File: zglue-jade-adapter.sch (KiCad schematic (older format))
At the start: 63 parts, among them J1 543630489, J2 543630489

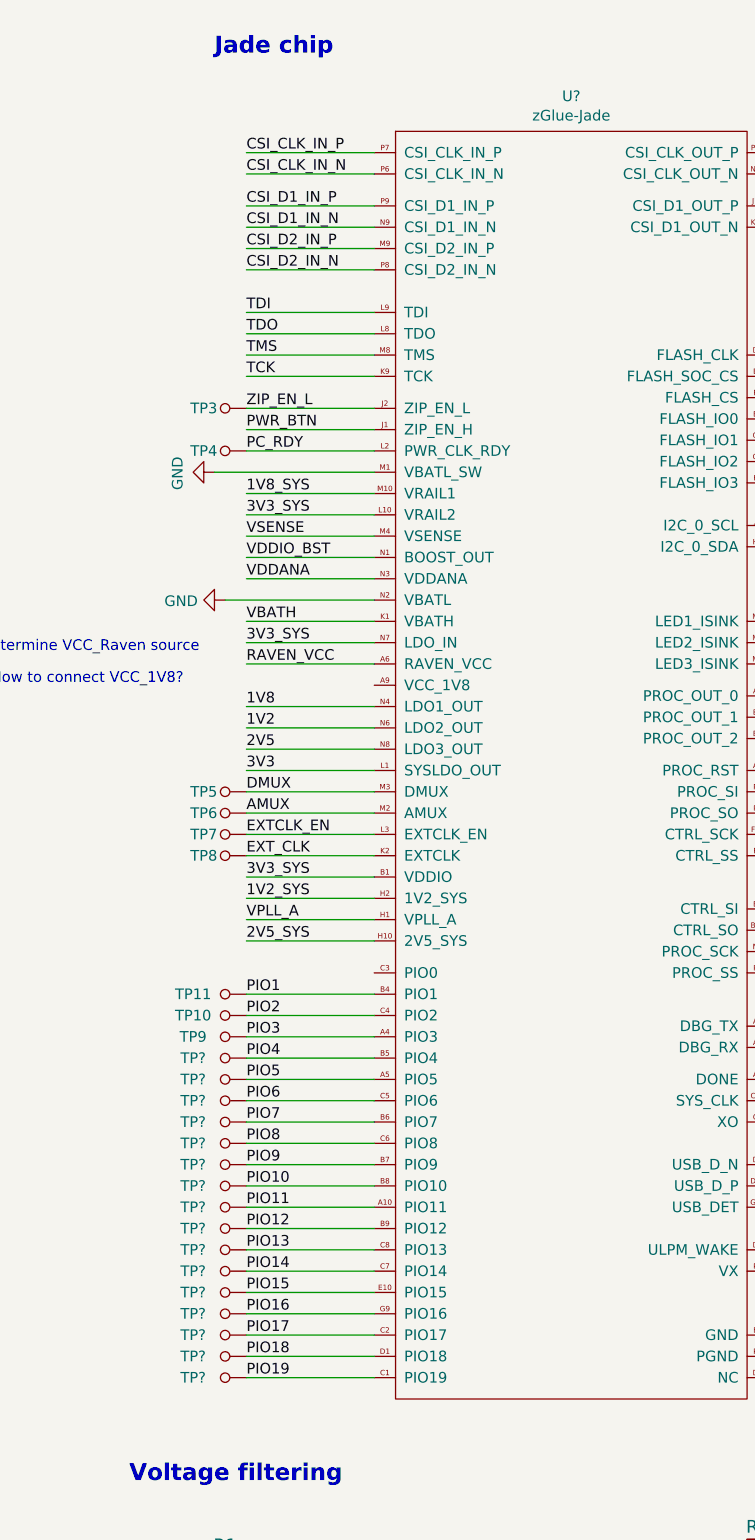
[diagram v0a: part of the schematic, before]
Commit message: Add component placement
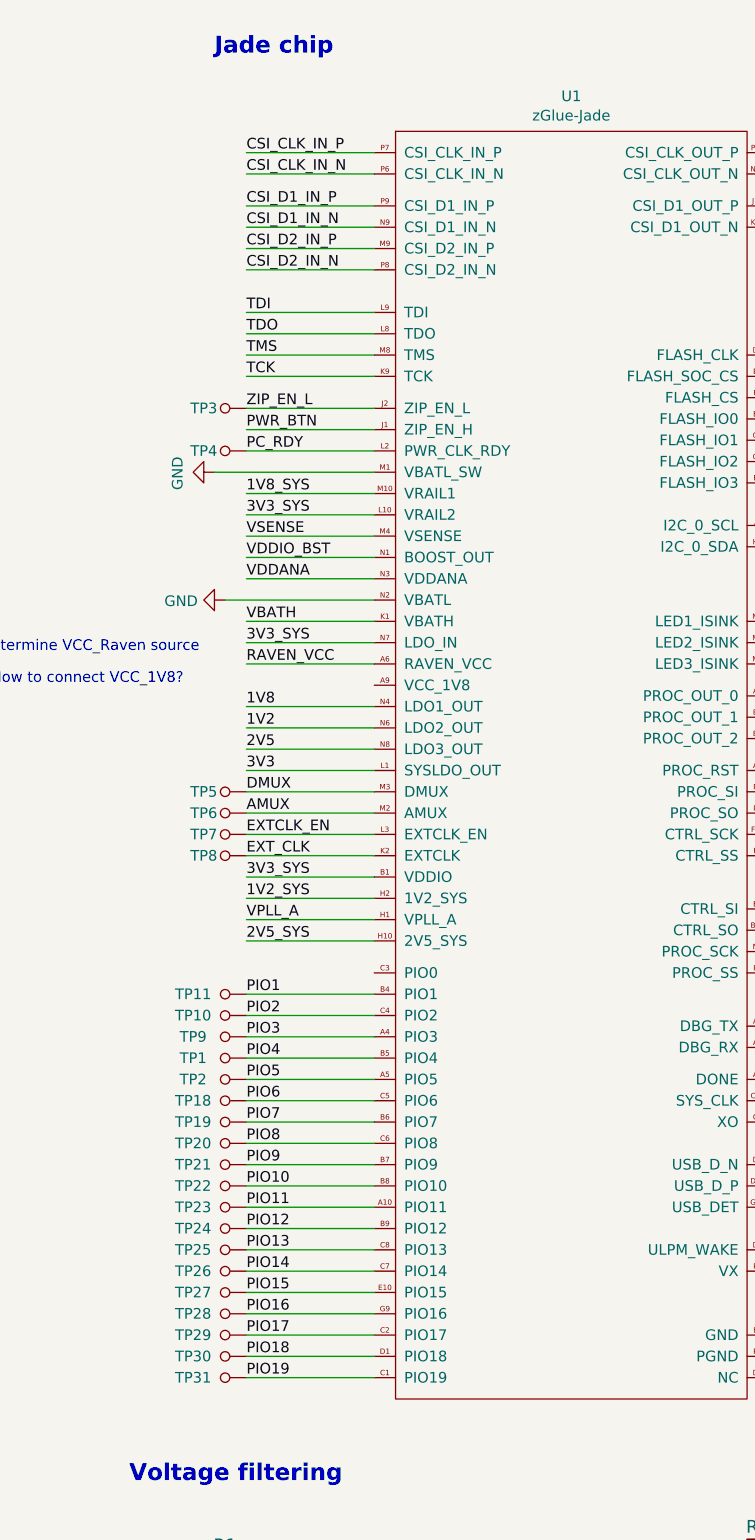
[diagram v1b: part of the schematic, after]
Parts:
- U1: renamed from U?; footprint (none) -> lib:Z-Glue_LGA-96
- gave numbers to parts that had none: 16
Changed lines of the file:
@@
 $EndComp
 $Comp
-L power:GND #PWR?
+L power:GND #PWR0101
 U 1 1 5DBC7F26
 P 1600 2800
-F 0 "#PWR?" H 1600 2550 50  0001 C CNN
+F 0 "#PWR0101" H 1600 2550 50  0001 C CNN
 F 1 "GND" H 1605 2627 50  0000 C CNN
 F 2 "" H 1600 2800 50  0001 C CNN
@@
 RAVEN_VCC
 $Comp
-L power:GND #PWR?
+L power:GND #PWR0102
 U 1 1 5E01A99B
 P 4450 7100
-F 0 "#PWR?" H 4450 6850 50  0001 C CNN
+F 0 "#PWR0102" H 4450 6850 50  0001 C CNN
 F 1 "GND" H 4455 6927 50  0000 C CNN
 F 2 "" H 4450 7100 50  0001 C CNN
@@
 	2350 5650 1750 5650
 $Comp
-L antmicroTestPoints:TP_SMD1MM TP?
+L antmicroTestPoints:TP_SMD1MM TP18
 U 1 1 5E08B0EF
 P 1650 5750
-F 0 "TP?" V 1650 5600 50  0000 C CNN
+F 0 "TP18" V 1650 5600 50  0000 C CNN
 F 1 "TP_SMD1MM" H 1650 5650 50  0001 C CNN
 F 2 "antmicro-footprints:Testpoint_smd_1mm" H 1850 5950 60  0001 L CNN
@@
 $EndComp
 $Comp
-L antmicroTestPoints:TP_SMD1MM TP?
+L antmicroTestPoints:TP_SMD1MM TP2
 U 1 1 5E08B0F6
 P 1650 5650
-F 0 "TP?" V 1650 5500 50  0000 C CNN
+F 0 "TP2" V 1650 5500 50  0000 C CNN
 F 1 "TP_SMD1MM" H 1650 5550 50  0001 C CNN
 F 2 "antmicro-footprints:Testpoint_smd_1mm" H 1850 5850 60  0001 L CNN
@@
 $EndComp
 $Comp
-L antmicroTestPoints:TP_SMD1MM TP?
+L antmicroTestPoints:TP_SMD1MM TP1
 U 1 1 5E08B0FD
 P 1650 5550
-F 0 "TP?" V 1650 5400 50  0000 C CNN
+F 0 "TP1" V 1650 5400 50  0000 C CNN
 F 1 "TP_SMD1MM" H 1650 5450 50  0001 C CNN
 F 2 "antmicro-footprints:Testpoint_smd_1mm" H 1850 5750 60  0001 L CNN
@@
 	2350 5950 1750 5950
 $Comp
-L antmicroTestPoints:TP_SMD1MM TP?
+L antmicroTestPoints:TP_SMD1MM TP21
 U 1 1 5E09E6BC
 P 1650 6050
-F 0 "TP?" V 1650 5900 50  0000 C CNN
+F 0 "TP21" V 1650 5900 50  0000 C CNN
 F 1 "TP_SMD1MM" H 1650 5950 50  0001 C CNN
 F 2 "antmicro-footprints:Testpoint_smd_1mm" H 1850 6250 60  0001 L CNN
@@
 $EndComp
 $Comp
-L antmicroTestPoints:TP_SMD1MM TP?
+L antmicroTestPoints:TP_SMD1MM TP20
 U 1 1 5E09E6C3
 P 1650 5950
-F 0 "TP?" V 1650 5800 50  0000 C CNN
+F 0 "TP20" V 1650 5800 50  0000 C CNN
 F 1 "TP_SMD1MM" H 1650 5850 50  0001 C CNN
 F 2 "antmicro-footprints:Testpoint_smd_1mm" H 1850 6150 60  0001 L CNN
@@
 $EndComp
 $Comp
-L antmicroTestPoints:TP_SMD1MM TP?
+L antmicroTestPoints:TP_SMD1MM TP19
 U 1 1 5E09E6CA
 P 1650 5850
-F 0 "TP?" V 1650 5700 50  0000 C CNN
+F 0 "TP19" V 1650 5700 50  0000 C CNN
 F 1 "TP_SMD1MM" H 1650 5750 50  0001 C CNN
 F 2 "antmicro-footprints:Testpoint_smd_1mm" H 1850 6050 60  0001 L CNN
@@
 	2350 6250 1750 6250
 $Comp
-L antmicroTestPoints:TP_SMD1MM TP?
+L antmicroTestPoints:TP_SMD1MM TP24
 U 1 1 5E0B2973
 P 1650 6350
-F 0 "TP?" V 1650 6200 50  0000 C CNN
+F 0 "TP24" V 1650 6200 50  0000 C CNN
 F 1 "TP_SMD1MM" H 1650 6250 50  0001 C CNN
 F 2 "antmicro-footprints:Testpoint_smd_1mm" H 1850 6550 60  0001 L CNN
@@
 $EndComp
 $Comp
-L antmicroTestPoints:TP_SMD1MM TP?
+L antmicroTestPoints:TP_SMD1MM TP23
 U 1 1 5E0B297A
 P 1650 6250
-F 0 "TP?" V 1650 6100 50  0000 C CNN
+F 0 "TP23" V 1650 6100 50  0000 C CNN
 F 1 "TP_SMD1MM" H 1650 6150 50  0001 C CNN
 F 2 "antmicro-footprints:Testpoint_smd_1mm" H 1850 6450 60  0001 L CNN
@@
 $EndComp
 $Comp
-L antmicroTestPoints:TP_SMD1MM TP?
+L antmicroTestPoints:TP_SMD1MM TP22
 U 1 1 5E0B2981
 P 1650 6150
-F 0 "TP?" V 1650 6000 50  0000 C CNN
+F 0 "TP22" V 1650 6000 50  0000 C CNN
 F 1 "TP_SMD1MM" H 1650 6050 50  0001 C CNN
 F 2 "antmicro-footprints:Testpoint_smd_1mm" H 1850 6350 60  0001 L CNN
@@
 	2350 6550 1750 6550
 $Comp
-L antmicroTestPoints:TP_SMD1MM TP?
+L antmicroTestPoints:TP_SMD1MM TP27
 U 1 1 5E0C7911
 P 1650 6650
-F 0 "TP?" V 1650 6500 50  0000 C CNN
+F 0 "TP27" V 1650 6500 50  0000 C CNN
 F 1 "TP_SMD1MM" H 1650 6550 50  0001 C CNN
 F 2 "antmicro-footprints:Testpoint_smd_1mm" H 1850 6850 60  0001 L CNN
@@
 $EndComp
 $Comp
-L antmicroTestPoints:TP_SMD1MM TP?
+L antmicroTestPoints:TP_SMD1MM TP26
 U 1 1 5E0C7918
 P 1650 6550
-F 0 "TP?" V 1650 6400 50  0000 C CNN
+F 0 "TP26" V 1650 6400 50  0000 C CNN
 F 1 "TP_SMD1MM" H 1650 6450 50  0001 C CNN
 F 2 "antmicro-footprints:Testpoint_smd_1mm" H 1850 6750 60  0001 L CNN
@@
 $EndComp
 $Comp
-L antmicroTestPoints:TP_SMD1MM TP?
+L antmicroTestPoints:TP_SMD1MM TP25
 U 1 1 5E0C791F
 P 1650 6450
-F 0 "TP?" V 1650 6300 50  0000 C CNN
+F 0 "TP25" V 1650 6300 50  0000 C CNN
 F 1 "TP_SMD1MM" H 1650 6350 50  0001 C CNN
 F 2 "antmicro-footprints:Testpoint_smd_1mm" H 1850 6650 60  0001 L CNN
@@
 	2350 6850 1750 6850
 $Comp
-L antmicroTestPoints:TP_SMD1MM TP?
+L antmicroTestPoints:TP_SMD1MM TP30
 U 1 1 5E0DD59F
 P 1650 6950
-F 0 "TP?" V 1650 6800 50  0000 C CNN
+F 0 "TP30" V 1650 6800 50  0000 C CNN
 F 1 "TP_SMD1MM" H 1650 6850 50  0001 C CNN
 F 2 "antmicro-footprints:Testpoint_smd_1mm" H 1850 7150 60  0001 L CNN
@@
 $EndComp
 $Comp
-L antmicroTestPoints:TP_SMD1MM TP?
+L antmicroTestPoints:TP_SMD1MM TP29
 U 1 1 5E0DD5A6
 P 1650 6850
-F 0 "TP?" V 1650 6700 50  0000 C CNN
+F 0 "TP29" V 1650 6700 50  0000 C CNN
 F 1 "TP_SMD1MM" H 1650 6750 50  0001 C CNN
 F 2 "antmicro-footprints:Testpoint_smd_1mm" H 1850 7050 60  0001 L CNN
@@
 $EndComp
 $Comp
-L antmicroTestPoints:TP_SMD1MM TP?
+L antmicroTestPoints:TP_SMD1MM TP28
 U 1 1 5E0DD5AD
 P 1650 6750
-F 0 "TP?" V 1650 6600 50  0000 C CNN
+F 0 "TP28" V 1650 6600 50  0000 C CNN
 F 1 "TP_SMD1MM" H 1650 6650 50  0001 C CNN
 F 2 "antmicro-footprints:Testpoint_smd_1mm" H 1850 6950 60  0001 L CNN
@@
 	2350 7050 1750 7050
 $Comp
-L antmicroTestPoints:TP_SMD1MM TP?
+L antmicroTestPoints:TP_SMD1MM TP31
 U 1 1 5E0F3F70
 P 1650 7050
-F 0 "TP?" V 1650 6900 50  0000 C CNN
+F 0 "TP31" V 1650 6900 50  0000 C CNN
 F 1 "TP_SMD1MM" H 1650 6950 50  0001 C CNN
 F 2 "antmicro-footprints:Testpoint_smd_1mm" H 1850 7250 60  0001 L CNN
@@
 PIO19
 $Comp
-L zglue-jade:zGlue-Jade U?
+L zglue-jade:zGlue-Jade U1
 U 1 1 5DB41B4F
 P 3200 3450
-F 0 "U?" H 3275 5865 50  0000 C CNN
+F 0 "U1" H 3275 5865 50  0000 C CNN
 F 1 "zGlue-Jade" H 3275 5774 50  0000 C CNN
-F 2 "" H 3200 3450 50  0001 C CNN
+F 2 "lib:Z-Glue_LGA-96" H 3200 3450 50  0001 C CNN
 F 3 "" H 3200 3450 50  0001 C CNN
 	1    3200 3450
